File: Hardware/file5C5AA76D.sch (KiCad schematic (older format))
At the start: 11 parts, among them J13 Conn_01x04_Female, U6 74HC595, U7 74HC595, U8 SID, X1 ACO-xxxMHz

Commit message: Started board layout
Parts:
- C29, C30: footprint (none) -> Capacitors_Tantalum_SMD:CP_Tantalum_Case-R_EIA-2012-12_Reflow
- C31: footprint (none) -> Capacitors_SMD:C_0603
- C32: footprint (none) -> Capacitors_SMD:CP_Elec_10x10
- U6, U7: footprint (none) -> Housings_SOIC:SOIC-16_3.9x9.9mm_Pitch1.27mm
- U8: footprint (none) -> Housings_DIP:DIP-28_W15.24mm_Socket; symbol SID_Parts:SID -> EuroSID-rescue:SID-SID_Parts
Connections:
- no-connect marks 0 -> 6
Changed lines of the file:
@@
 $EndDescr
 $Comp
-L SID_Parts:SID U?
+L EuroSID-rescue:SID-SID_Parts U?
 U 1 1 5C5AD583
 P 7100 2750
@@
 F 0 "U8" H 7075 3575 50  0000 C CNN
 F 1 "SID" H 7075 3484 50  0000 C CNN
-F 2 "" H 6850 3300 50  0001 C CNN
+F 2 "Housings_DIP:DIP-28_W15.24mm_Socket" H 6850 3300 50  0001 C CNN
 F 3 "" H 6850 3300 50  0001 C CNN
 	1    7100 2750
@@
 F 0 "U7" H 5300 5500 50  0000 C CNN
 F 1 "74HC595" H 5550 4800 50  0000 C CNN
-F 2 "" H 5300 5500 50  0001 C CNN
+F 2 "Housings_SOIC:SOIC-16_3.9x9.9mm_Pitch1.27mm" H 5300 5500 50  0001 C CNN
 F 3 "http://www.ti.com/lit/ds/symlink/sn74hc595.pdf" H 5300 5500 50  0001 C CNN
 	1    5300 5500
@@
 F 0 "U6" H 4400 4500 50  0000 C CNN
 F 1 "74HC595" H 4100 3850 50  0000 C CNN
-F 2 "" H 4400 4550 50  0001 C CNN
+F 2 "Housings_SOIC:SOIC-16_3.9x9.9mm_Pitch1.27mm" H 4400 4550 50  0001 C CNN
 F 3 "http://www.ti.com/lit/ds/symlink/sn74hc595.pdf" H 4400 4550 50  0001 C CNN
 	1    4400 4550
@@
 F 0 "C29" V 7945 2250 50  0000 C CNN
 F 1 "1 uF" V 8036 2250 50  0000 C CNN
-F 2 "" H 8238 2100 50  0001 C CNN
+F 2 "Capacitors_Tantalum_SMD:CP_Tantalum_Case-R_EIA-2012-12_Reflow" H 8238 2100 50  0001 C CNN
 F 3 "~" H 8200 2250 50  0001 C CNN
 	1    8200 2250
@@
 F 0 "C30" V 7945 2650 50  0000 C CNN
 F 1 "1 uF" V 8036 2650 50  0000 C CNN
-F 2 "" H 8238 2500 50  0001 C CNN
+F 2 "Capacitors_Tantalum_SMD:CP_Tantalum_Case-R_EIA-2012-12_Reflow" H 8238 2500 50  0001 C CNN
 F 3 "~" H 8200 2650 50  0001 C CNN
 	1    8200 2650
@@
 F 0 "C31" H 9315 2646 50  0000 L CNN
 F 1 "100 nF" H 9315 2555 50  0000 L CNN
-F 2 "" H 9238 2450 50  0001 C CNN
+F 2 "Capacitors_SMD:C_0603" H 9238 2450 50  0001 C CNN
 F 3 "~" H 9200 2600 50  0001 C CNN
 	1    9200 2600
@@
 F 0 "C32" H 9818 2646 50  0000 L CNN
 F 1 "2200 uF" H 9818 2555 50  0000 L CNN
-F 2 "" H 9738 2450 50  0001 C CNN
+F 2 "Capacitors_SMD:CP_Elec_10x10" H 9738 2450 50  0001 C CNN
 F 3 "~" H 9700 2600 50  0001 C CNN
 	1    9700 2600
@@
 Wire Wire Line
 	5150 2650 6650 2650
+NoConn ~ 5700 5600
+NoConn ~ 5700 5700
+NoConn ~ 5700 5800
+NoConn ~ 5700 6000
+NoConn ~ 7500 2550
+NoConn ~ 7500 2650
 Wire Bus Line
 	6200 3050 6200 4050

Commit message: Fixed issues with footprints
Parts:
- C29, C30: footprint Capacitors_Tantalum_SMD:CP_Tantalum_Case-R_EIA-2012-12_Reflow -> Capacitor_Tantalum_SMD:CP_EIA-2012-12_Kemet-R
- C31: footprint Capacitors_SMD:C_0603 -> Capacitor_SMD:C_0603_1608Metric
- C32: footprint Capacitors_SMD:CP_Elec_10x10 -> Capacitor_SMD:CP_Elec_10x10
- U6, U7: footprint Housings_SOIC:SOIC-16_3.9x9.9mm_Pitch1.27mm -> Package_SO:SOIC-16_3.9x9.9mm_P1.27mm
- U8: footprint Housings_DIP:DIP-28_W15.24mm_Socket -> Package_DIP:DIP-28_W15.24mm_Socket
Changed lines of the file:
@@
 F 0 "U8" H 7075 3575 50  0000 C CNN
 F 1 "SID" H 7075 3484 50  0000 C CNN
-F 2 "Housings_DIP:DIP-28_W15.24mm_Socket" H 6850 3300 50  0001 C CNN
+F 2 "Package_DIP:DIP-28_W15.24mm_Socket" H 6850 3300 50  0001 C CNN
 F 3 "" H 6850 3300 50  0001 C CNN
 	1    7100 2750
@@
 F 0 "U7" H 5300 5500 50  0000 C CNN
 F 1 "74HC595" H 5550 4800 50  0000 C CNN
-F 2 "Housings_SOIC:SOIC-16_3.9x9.9mm_Pitch1.27mm" H 5300 5500 50  0001 C CNN
+F 2 "Package_SO:SOIC-16_3.9x9.9mm_P1.27mm" H 5300 5500 50  0001 C CNN
 F 3 "http://www.ti.com/lit/ds/symlink/sn74hc595.pdf" H 5300 5500 50  0001 C CNN
 	1    5300 5500
@@
 F 0 "U6" H 4400 4500 50  0000 C CNN
 F 1 "74HC595" H 4100 3850 50  0000 C CNN
-F 2 "Housings_SOIC:SOIC-16_3.9x9.9mm_Pitch1.27mm" H 4400 4550 50  0001 C CNN
+F 2 "Package_SO:SOIC-16_3.9x9.9mm_P1.27mm" H 4400 4550 50  0001 C CNN
 F 3 "http://www.ti.com/lit/ds/symlink/sn74hc595.pdf" H 4400 4550 50  0001 C CNN
 	1    4400 4550
@@
 F 0 "C29" V 7945 2250 50  0000 C CNN
 F 1 "1 uF" V 8036 2250 50  0000 C CNN
-F 2 "Capacitors_Tantalum_SMD:CP_Tantalum_Case-R_EIA-2012-12_Reflow" H 8238 2100 50  0001 C CNN
+F 2 "Capacitor_Tantalum_SMD:CP_EIA-2012-12_Kemet-R" H 8238 2100 50  0001 C CNN
 F 3 "~" H 8200 2250 50  0001 C CNN
 	1    8200 2250
@@
 F 0 "C30" V 7945 2650 50  0000 C CNN
 F 1 "1 uF" V 8036 2650 50  0000 C CNN
-F 2 "Capacitors_Tantalum_SMD:CP_Tantalum_Case-R_EIA-2012-12_Reflow" H 8238 2500 50  0001 C CNN
+F 2 "Capacitor_Tantalum_SMD:CP_EIA-2012-12_Kemet-R" H 8238 2500 50  0001 C CNN
 F 3 "~" H 8200 2650 50  0001 C CNN
 	1    8200 2650
@@
 F 0 "C31" H 9315 2646 50  0000 L CNN
 F 1 "100 nF" H 9315 2555 50  0000 L CNN
-F 2 "Capacitors_SMD:C_0603" H 9238 2450 50  0001 C CNN
+F 2 "Capacitor_SMD:C_0603_1608Metric" H 9238 2450 50  0001 C CNN
 F 3 "~" H 9200 2600 50  0001 C CNN
 	1    9200 2600
@@
 F 0 "C32" H 9818 2646 50  0000 L CNN
 F 1 "2200 uF" H 9818 2555 50  0000 L CNN
-F 2 "Capacitors_SMD:CP_Elec_10x10" H 9738 2450 50  0001 C CNN
+F 2 "Capacitor_SMD:CP_Elec_10x10" H 9738 2450 50  0001 C CNN
 F 3 "~" H 9700 2600 50  0001 C CNN
 	1    9700 2600

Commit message: Added PJ398SM model
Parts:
- R49: footprint (none) -> Resistor_SMD:R_0603_1608Metric
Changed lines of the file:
@@
 F 0 "R49" H 7970 2146 50  0000 L CNN
 F 1 "1K" H 7970 2055 50  0000 L CNN
-F 2 "" V 7830 2100 50  0001 C CNN
+F 2 "Resistor_SMD:R_0603_1608Metric" V 7830 2100 50  0001 C CNN
 F 3 "~" H 7900 2100 50  0001 C CNN
 	1    7900 2100

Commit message: Finished assigning footprints
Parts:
- removed X1: ACO-xxxMHz, Oscillator:Oscillator_DIP-14, symbol Oscillator:ACO-xxxMHz
- added X1: ECS-8FMX-010-TR, Oscillator:Oscillator_SMD_Abracon_ASV-4Pin_7.0x5.1mm, symbol Oscillator:ASV-xxxMHz
- J13: footprint (none) -> Connector_PinHeader_2.54mm:PinHeader_1x04_P2.54mm_Vertical
- JP1: footprint (none) -> Connector_PinHeader_2.54mm:PinHeader_1x03_P2.54mm_Vertical
- R49: value 1K -> 1k
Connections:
- wire segments 85 -> 89
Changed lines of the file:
@@
-$EndComp
-$Comp
-L Oscillator:ACO-xxxMHz X?
-U 1 1 5C5AD58A
-P 4850 2650
-AR Path="/5C5AD58A" Ref="X?"  Part="1"
-AR Path="/5C5AA76E/5C5AD58A" Ref="X1"  Part="1"
-F 0 "X1" H 4510 2696 50  0000 R CNN
-F 1 "ACO-xxxMHz" H 4510 2605 50  0000 R CNN
-F 2 "Oscillator:Oscillator_DIP-14" H 5300 2300 50  0001 C CNN
-F 3 "http://www.conwin.com/datasheets/cx/cx030.pdf" H 4750 2650 50  0001 C CNN
-	1    4850 2650
-	1    0    0    -1
 $EndComp
 $Comp
@@
 $EndComp
 Wire Wire Line
-	4850 2350 4850 2200
+	4850 2350 4850 2300
 $Comp
 L power:+5V #PWR?
@@
 F 0 "JP1" H 7750 1704 50  0000 C CNN
 F 1 "Jumper_3_Bridged12" H 7750 1600 50  0000 C CNN
-F 2 "" H 7750 1500 50  0001 C CNN
+F 2 "Connector_PinHeader_2.54mm:PinHeader_1x03_P2.54mm_Vertical" H 7750 1500 50  0001 C CNN
 F 3 "~" H 7750 1500 50  0001 C CNN
 	1    7750 1500
@@
 F 0 "J13" H 6344 1925 50  0000 C CNN
 F 1 "Conn_01x04_Female" H 6344 2016 50  0000 C CNN
-F 2 "" H 6450 2350 50  0001 C CNN
+F 2 "Connector_PinHeader_2.54mm:PinHeader_1x04_P2.54mm_Vertical" H 6450 2350 50  0001 C CNN
 F 3 "~" H 6450 2350 50  0001 C CNN
 	1    6450 2350
@@
 AR Path="/5C5AA76E/5C5AD648" Ref="R49"  Part="1"
 F 0 "R49" H 7970 2146 50  0000 L CNN
-F 1 "1K" H 7970 2055 50  0000 L CNN
+F 1 "1k" H 7970 2055 50  0000 L CNN
 F 2 "Resistor_SMD:R_0603_1608Metric" V 7830 2100 50  0001 C CNN
 F 3 "~" H 7900 2100 50  0001 C CNN
@@
 NoConn ~ 7500 2550
 NoConn ~ 7500 2650
+$Comp
+L Oscillator:ASV-xxxMHz X1
+U 1 1 5BE68FC3
+P 4850 2650
+F 0 "X1" H 5191 2696 50  0000 L CNN
+F 1 "ECS-8FMX-010-TR" H 5191 2605 50  0000 L CNN
+F 2 "Oscillator:Oscillator_SMD_Abracon_ASV-4Pin_7.0x5.1mm" H 5550 2300 50  0001 C CNN
+F 3 "http://www.abracon.com/Oscillators/ASV.pdf" H 4750 2650 50  0001 C CNN
+	1    4850 2650
+	1    0    0    -1
+$EndComp
+Wire Wire Line
+	4550 2650 4300 2650
+Wire Wire Line
+	4300 2650 4300 2300
+Wire Wire Line
+	4300 2300 4850 2300
 Wire Bus Line
 	6200 3050 6200 4050
@@
 Wire Bus Line
 	6200 4050 6200 5400
+Connection ~ 4850 2300
+Wire Wire Line
+	4850 2300 4850 2200
 $EndSCHEMATC

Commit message: Updated schematic
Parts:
- renumbered C29 to C35, C30 to C36, C31 to C37, C32 to C38, J13 to J14, R49 to R53
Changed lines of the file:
@@
 P 4850 3200
 AR Path="/5C5AD591" Ref="#PWR?"  Part="1"
-AR Path="/5C5AA76E/5C5AD591" Ref="#PWR0192"  Part="1"
-F 0 "#PWR0192" H 4850 2950 50  0001 C CNN
+AR Path="/5C5AA76E/5C5AD591" Ref="#PWR0107"  Part="1"
+F 0 "#PWR0107" H 4850 2950 50  0001 C CNN
 F 1 "GND" H 4855 3027 50  0000 C CNN
 F 2 "" H 4850 3200 50  0001 C CNN
@@
 P 6550 3550
 AR Path="/5C5AD597" Ref="#PWR?"  Part="1"
-AR Path="/5C5AA76E/5C5AD597" Ref="#PWR0193"  Part="1"
-F 0 "#PWR0193" H 6550 3300 50  0001 C CNN
+AR Path="/5C5AA76E/5C5AD597" Ref="#PWR0110"  Part="1"
+F 0 "#PWR0110" H 6550 3300 50  0001 C CNN
 F 1 "GND" H 6555 3377 50  0000 C CNN
 F 2 "" H 6550 3550 50  0001 C CNN
@@
 P 4850 2200
 AR Path="/5C5AD5A0" Ref="#PWR?"  Part="1"
-AR Path="/5C5AA76E/5C5AD5A0" Ref="#PWR0194"  Part="1"
-F 0 "#PWR0194" H 4850 2050 50  0001 C CNN
+AR Path="/5C5AA76E/5C5AD5A0" Ref="#PWR0106"  Part="1"
+F 0 "#PWR0106" H 4850 2050 50  0001 C CNN
 F 1 "+5V" H 4865 2373 50  0000 C CNN
 F 2 "" H 4850 2200 50  0001 C CNN
@@
 P 9200 1500
 AR Path="/5C5AD5A7" Ref="#PWR?"  Part="1"
-AR Path="/5C5AA76E/5C5AD5A7" Ref="#PWR0195"  Part="1"
-F 0 "#PWR0195" H 9200 1350 50  0001 C CNN
+AR Path="/5C5AA76E/5C5AD5A7" Ref="#PWR0114"  Part="1"
+F 0 "#PWR0114" H 9200 1350 50  0001 C CNN
 F 1 "+5V" H 9215 1673 50  0000 C CNN
 F 2 "" H 9200 1500 50  0001 C CNN
@@
 P 7250 1500
 AR Path="/5C5AD5AF" Ref="#PWR?"  Part="1"
-AR Path="/5C5AA76E/5C5AD5AF" Ref="#PWR0196"  Part="1"
-F 0 "#PWR0196" H 7250 1350 50  0001 C CNN
+AR Path="/5C5AA76E/5C5AD5AF" Ref="#PWR0111"  Part="1"
+F 0 "#PWR0111" H 7250 1350 50  0001 C CNN
 F 1 "+12V" H 7265 1673 50  0000 C CNN
 F 2 "" H 7250 1500 50  0001 C CNN
@@
 P 8300 1500
 AR Path="/5C5AD5B5" Ref="#PWR?"  Part="1"
-AR Path="/5C5AA76E/5C5AD5B5" Ref="#PWR0197"  Part="1"
-F 0 "#PWR0197" H 8300 1350 50  0001 C CNN
+AR Path="/5C5AA76E/5C5AD5B5" Ref="#PWR0113"  Part="1"
+F 0 "#PWR0113" H 8300 1350 50  0001 C CNN
 F 1 "+9V" H 8315 1673 50  0000 C CNN
 F 2 "" H 8300 1500 50  0001 C CNN
@@
 P 6450 2350
 AR Path="/5C5AD5C8" Ref="J?"  Part="1"
-AR Path="/5C5AA76E/5C5AD5C8" Ref="J13"  Part="1"
-F 0 "J13" H 6344 1925 50  0000 C CNN
+AR Path="/5C5AA76E/5C5AD5C8" Ref="J14"  Part="1"
+F 0 "J14" H 6344 1925 50  0000 C CNN
 F 1 "Conn_01x04_Female" H 6344 2016 50  0000 C CNN
 F 2 "Connector_PinHeader_2.54mm:PinHeader_1x04_P2.54mm_Vertical" H 6450 2350 50  0001 C CNN
@@
 P 4850 3750
 AR Path="/5C5AD5CF" Ref="#PWR?"  Part="1"
-AR Path="/5C5AA76E/5C5AD5CF" Ref="#PWR0198"  Part="1"
-F 0 "#PWR0198" H 4850 3600 50  0001 C CNN
+AR Path="/5C5AA76E/5C5AD5CF" Ref="#PWR0108"  Part="1"
+F 0 "#PWR0108" H 4850 3600 50  0001 C CNN
 F 1 "+5V" H 4865 3923 50  0000 C CNN
 F 2 "" H 4850 3750 50  0001 C CNN
@@
 P 4800 6250
 AR Path="/5C5AD60E" Ref="#PWR?"  Part="1"
-AR Path="/5C5AA76E/5C5AD60E" Ref="#PWR0199"  Part="1"
-F 0 "#PWR0199" H 4800 6000 50  0001 C CNN
+AR Path="/5C5AA76E/5C5AD60E" Ref="#PWR0105"  Part="1"
+F 0 "#PWR0105" H 4800 6000 50  0001 C CNN
 F 1 "GND" H 4805 6077 50  0000 C CNN
 F 2 "" H 4800 6250 50  0001 C CNN
@@
 P 7900 2100
 AR Path="/5C5AD648" Ref="R?"  Part="1"
-AR Path="/5C5AA76E/5C5AD648" Ref="R49"  Part="1"
-F 0 "R49" H 7970 2146 50  0000 L CNN
+AR Path="/5C5AA76E/5C5AD648" Ref="R53"  Part="1"
+F 0 "R53" H 7970 2146 50  0000 L CNN
 F 1 "1k" H 7970 2055 50  0000 L CNN
 F 2 "Resistor_SMD:R_0603_1608Metric" V 7830 2100 50  0001 C CNN
@@
 P 7900 1900
 AR Path="/5C5AD64F" Ref="#PWR?"  Part="1"
-AR Path="/5C5AA76E/5C5AD64F" Ref="#PWR0200"  Part="1"
-F 0 "#PWR0200" H 7900 1650 50  0001 C CNN
+AR Path="/5C5AA76E/5C5AD64F" Ref="#PWR0112"  Part="1"
+F 0 "#PWR0112" H 7900 1650 50  0001 C CNN
 F 1 "GND" H 7905 1727 50  0000 C CNN
 F 2 "" H 7900 1900 50  0001 C CNN
@@
 P 5300 2750
 AR Path="/5C5AD68F" Ref="#PWR?"  Part="1"
-AR Path="/5C5AA76E/5C5AD68F" Ref="#PWR0201"  Part="1"
-F 0 "#PWR0201" H 5300 2500 50  0001 C CNN
+AR Path="/5C5AA76E/5C5AD68F" Ref="#PWR0109"  Part="1"
+F 0 "#PWR0109" H 5300 2500 50  0001 C CNN
 F 1 "GND" H 5305 2577 50  0000 C CNN
 F 2 "" H 5300 2750 50  0001 C CNN
@@
 	8400 2250 8550 2250
 $Comp
-L Device:CP C29
+L Device:CP C35
 U 1 1 5C5B7C97
 P 8200 2250
-F 0 "C29" V 7945 2250 50  0000 C CNN
+F 0 "C35" V 7945 2250 50  0000 C CNN
 F 1 "1 uF" V 8036 2250 50  0000 C CNN
 F 2 "Capacitor_Tantalum_SMD:CP_EIA-2012-12_Kemet-R" H 8238 2100 50  0001 C CNN
@@
 $EndComp
 $Comp
-L Device:CP C30
+L Device:CP C36
 U 1 1 5C5C287D
 P 8200 2650
-F 0 "C30" V 7945 2650 50  0000 C CNN
+F 0 "C36" V 7945 2650 50  0000 C CNN
 F 1 "1 uF" V 8036 2650 50  0000 C CNN
 F 2 "Capacitor_Tantalum_SMD:CP_EIA-2012-12_Kemet-R" H 8238 2500 50  0001 C CNN
@@
 $EndComp
 $Comp
-L Device:C C31
+L Device:C C37
 U 1 1 5BDE375F
 P 9200 2600
-F 0 "C31" H 9315 2646 50  0000 L CNN
+F 0 "C37" H 9315 2646 50  0000 L CNN
 F 1 "100 nF" H 9315 2555 50  0000 L CNN
 F 2 "Capacitor_SMD:C_0603_1608Metric" H 9238 2450 50  0001 C CNN
@@
 P 9200 2900
 AR Path="/5BDE37A7" Ref="#PWR?"  Part="1"
-AR Path="/5C5AA76E/5BDE37A7" Ref="#PWR0202"  Part="1"
-F 0 "#PWR0202" H 9200 2650 50  0001 C CNN
+AR Path="/5C5AA76E/5BDE37A7" Ref="#PWR0115"  Part="1"
+F 0 "#PWR0115" H 9200 2650 50  0001 C CNN
 F 1 "GND" H 9205 2727 50  0000 C CNN
 F 2 "" H 9200 2900 50  0001 C CNN
@@
 	9200 1500 9200 2450
 $Comp
-L Device:CP C32
+L Device:CP C38
 U 1 1 5BDEB869
 P 9700 2600
-F 0 "C32" H 9818 2646 50  0000 L CNN
+F 0 "C38" H 9818 2646 50  0000 L CNN
 F 1 "2200 uF" H 9818 2555 50  0000 L CNN
 F 2 "Capacitor_SMD:CP_Elec_10x10" H 9738 2450 50  0001 C CNN
@@
 P 9700 2900
 AR Path="/5BDEB8C2" Ref="#PWR?"  Part="1"
-AR Path="/5C5AA76E/5BDEB8C2" Ref="#PWR0203"  Part="1"
-F 0 "#PWR0203" H 9700 2650 50  0001 C CNN
+AR Path="/5C5AA76E/5BDEB8C2" Ref="#PWR0116"  Part="1"
+F 0 "#PWR0116" H 9700 2650 50  0001 C CNN
 F 1 "GND" H 9705 2727 50  0000 C CNN
 F 2 "" H 9700 2900 50  0001 C CNN
@@
 Wire Wire Line
 	4300 2300 4850 2300
+Connection ~ 4850 2300
+Wire Wire Line
+	4850 2300 4850 2200
 Wire Bus Line
 	6200 3050 6200 4050
@@
 Wire Bus Line
 	6200 4050 6200 5400
-Connection ~ 4850 2300
-Wire Wire Line
-	4850 2300 4850 2200
 $EndSCHEMATC

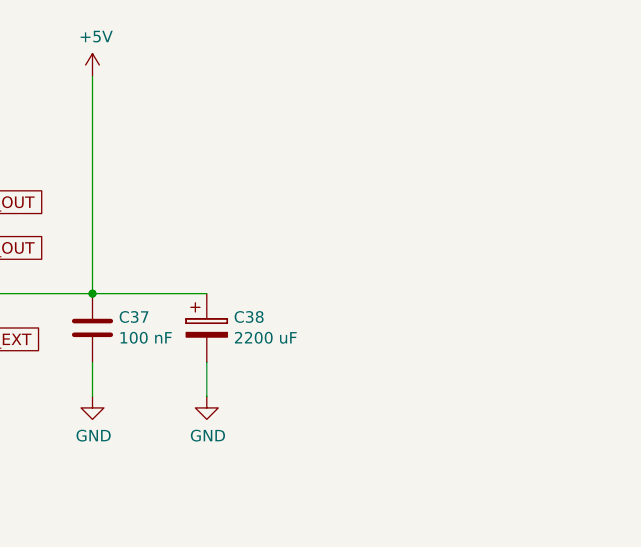
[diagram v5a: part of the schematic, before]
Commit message: Seperated two board with headers
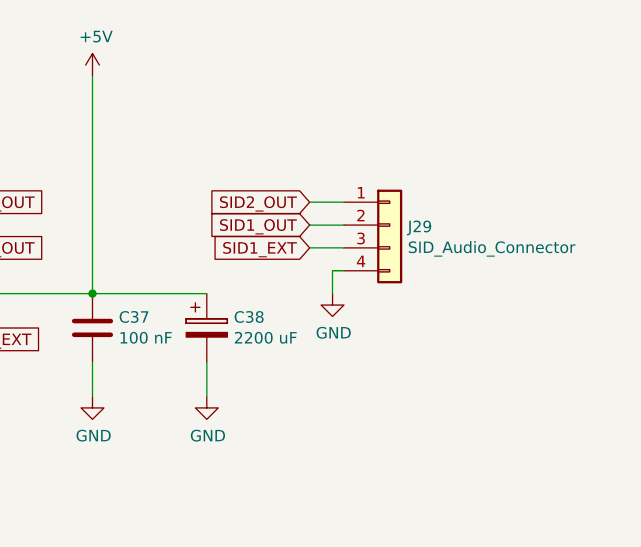
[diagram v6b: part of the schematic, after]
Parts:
- added J29: SID_Audio_Connector, Connector_PinHeader_2.54mm:PinHeader_1x04_P2.54mm_Vertical, symbol Connector_Generic:Conn_01x04
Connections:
- net GND: now also J29.4 (Pin_4)
- net SID1_EXT: now also J29.3 (Pin_3)
- net SID1_OUT: now also J29.1 (Pin_1), J29.2 (Pin_2)
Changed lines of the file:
@@
 Wire Wire Line
 	4850 2300 4850 2200
+$Comp
+L Connector_Generic:Conn_01x04 J29
+U 1 1 5C596EAE
+P 10500 2150
+F 0 "J29" H 10579 2142 50  0000 L CNN
+F 1 "SID_Audio_Connector" H 10579 2051 50  0000 L CNN
+F 2 "Connector_PinHeader_2.54mm:PinHeader_1x04_P2.54mm_Vertical" H 10500 2150 50  0001 C CNN
+F 3 "~" H 10500 2150 50  0001 C CNN
+	1    10500 2150
+	1    0    0    -1
+$EndComp
+Text GLabel 10150 2050 0    50   Input ~ 0
+SID2_OUT
+Text GLabel 10150 2150 0    50   Input ~ 0
+SID1_OUT
+Text GLabel 10150 2250 0    50   Input ~ 0
+SID1_EXT
+$Comp
+L power:GND #PWR?
+U 1 1 5C59702B
+P 10250 2450
+AR Path="/5C59702B" Ref="#PWR?"  Part="1"
+AR Path="/5C5AA76E/5C59702B" Ref="#PWR027"  Part="1"
+F 0 "#PWR027" H 10250 2200 50  0001 C CNN
+F 1 "GND" H 10255 2277 50  0000 C CNN
+F 2 "" H 10250 2450 50  0001 C CNN
+F 3 "" H 10250 2450 50  0001 C CNN
+	1    10250 2450
+	1    0    0    -1
+$EndComp
+Wire Wire Line
+	10250 2450 10250 2350
+Wire Wire Line
+	10250 2350 10300 2350
+Wire Wire Line
+	10150 2250 10300 2250
+Wire Wire Line
+	10150 2150 10300 2150
+Wire Wire Line
+	10150 2050 10300 2050
 Wire Bus Line
 	6200 3050 6200 4050

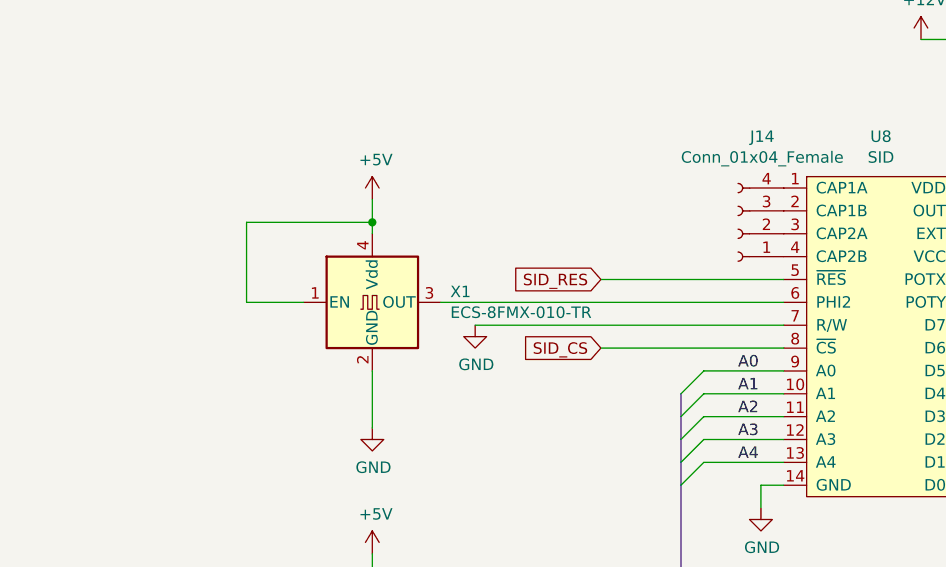
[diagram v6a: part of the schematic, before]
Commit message: Swapped for real oscillator, fixed footprint discrepencies
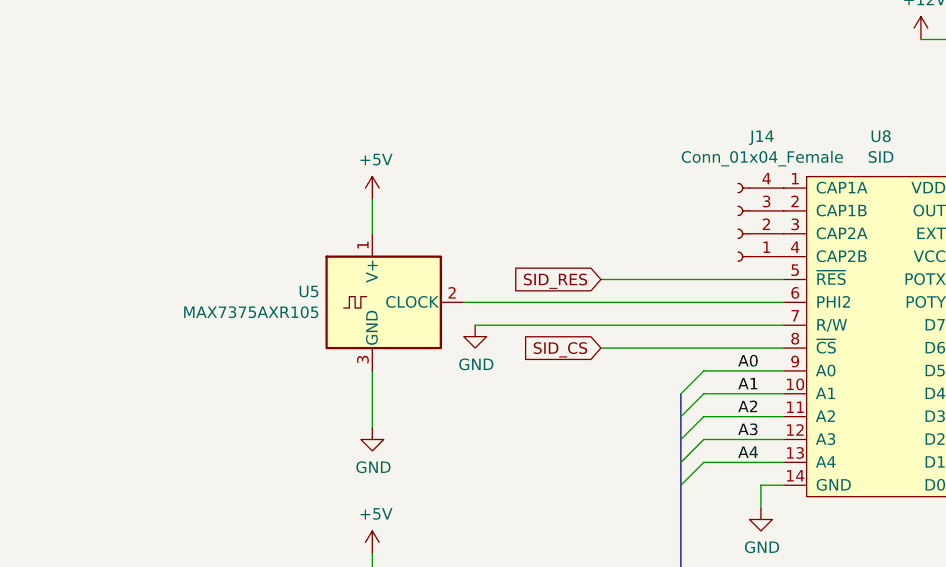
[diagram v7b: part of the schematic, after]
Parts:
- removed X1: ECS-8FMX-010-TR, Oscillator:Oscillator_SMD_Abracon_ASV-4Pin_7.0x5.1mm, symbol Oscillator:ASV-xxxMHz
- added U5: MAX7375AXR105, Package_TO_SOT_SMD:SOT-323_SC-70, symbol Oscillator:MAX7375AXR105
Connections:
- net +5V: now also U5.1 (V+)
- net GND: now also U5.3 (GND)
- net at U8.6 (PHI2): now also U5.2 (CLOCK)
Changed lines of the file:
@@
 	1    0    0    -1
 $EndComp
-Wire Wire Line
-	4850 2350 4850 2300
 $Comp
 L power:+5V #PWR?
@@
 	9700 2450 9200 2450
 Wire Wire Line
-	5150 2650 6650 2650
+	5250 2650 6650 2650
 NoConn ~ 5700 5600
 NoConn ~ 5700 5700
@@
 NoConn ~ 7500 2550
 NoConn ~ 7500 2650
-$Comp
-L Oscillator:ASV-xxxMHz X1
-U 1 1 5BE68FC3
-P 4850 2650
-F 0 "X1" H 5191 2696 50  0000 L CNN
-F 1 "ECS-8FMX-010-TR" H 5191 2605 50  0000 L CNN
-F 2 "Oscillator:Oscillator_SMD_Abracon_ASV-4Pin_7.0x5.1mm" H 5550 2300 50  0001 C CNN
-F 3 "http://www.abracon.com/Oscillators/ASV.pdf" H 4750 2650 50  0001 C CNN
-	1    4850 2650
-	1    0    0    -1
-$EndComp
-Wire Wire Line
-	4550 2650 4300 2650
-Wire Wire Line
-	4300 2650 4300 2300
-Wire Wire Line
-	4300 2300 4850 2300
-Connection ~ 4850 2300
-Wire Wire Line
-	4850 2300 4850 2200
 $Comp
 L Connector_Generic:Conn_01x04 J29
@@
 Wire Wire Line
 	10150 2050 10300 2050
+$Comp
+L Oscillator:MAX7375AXR105 U5
+U 1 1 5BF6505A
+P 4850 2650
+F 0 "U5" H 4620 2696 50  0000 R CNN
+F 1 "MAX7375AXR105" H 4620 2605 50  0000 R CNN
+F 2 "Package_TO_SOT_SMD:SOT-323_SC-70" H 5950 2300 50  0001 C CNN
+F 3 "https://datasheets.maximintegrated.com/en/ds/MAX7375.pdf" H 4750 2650 50  0001 C CNN
+	1    4850 2650
+	1    0    0    -1
+$EndComp
+Wire Wire Line
+	4850 2200 4850 2350
 Wire Bus Line
 	6200 3050 6200 4050
